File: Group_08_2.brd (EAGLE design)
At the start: 61 x 80 mm, 29 parts, among them J1 POWER_JACKPTH_LOCK, U1 +12v, U3 TCA9546ATSSOP, U4 TMUX1208

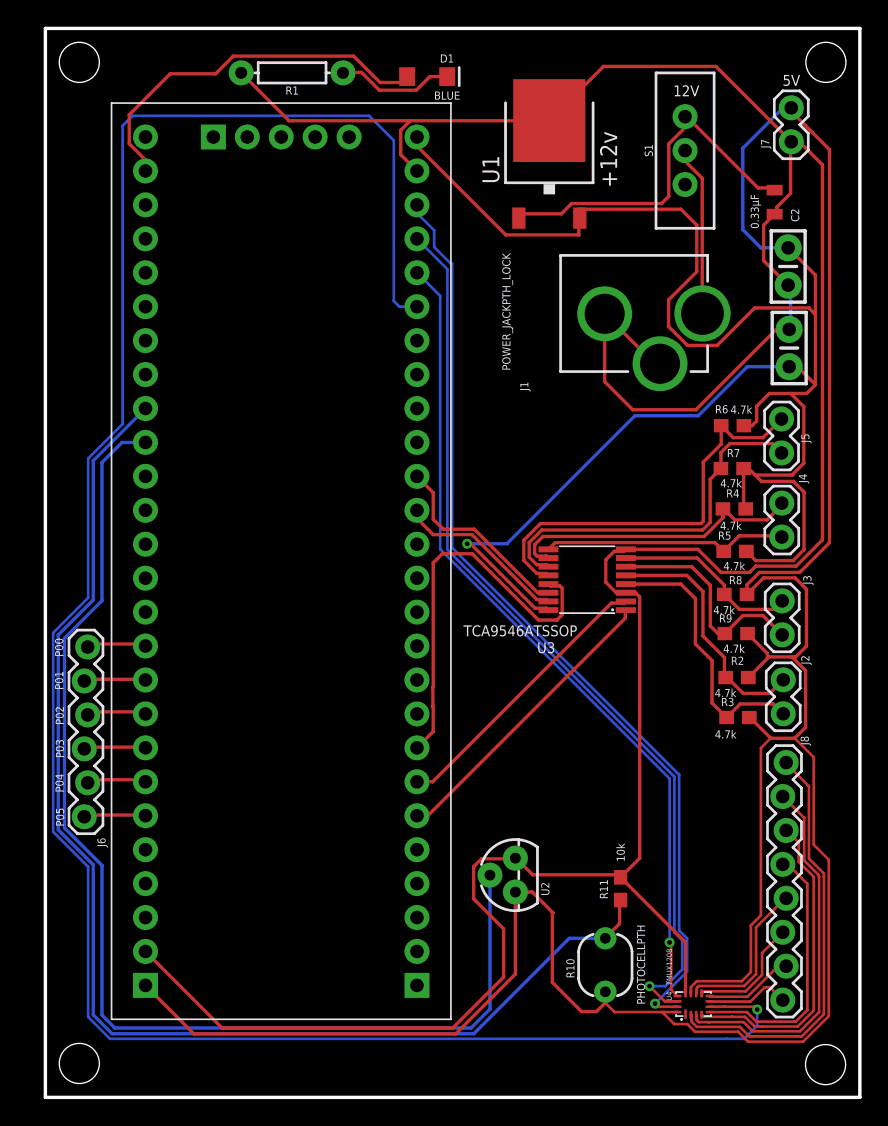
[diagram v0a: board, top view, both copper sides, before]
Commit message: completed routing of smaller board
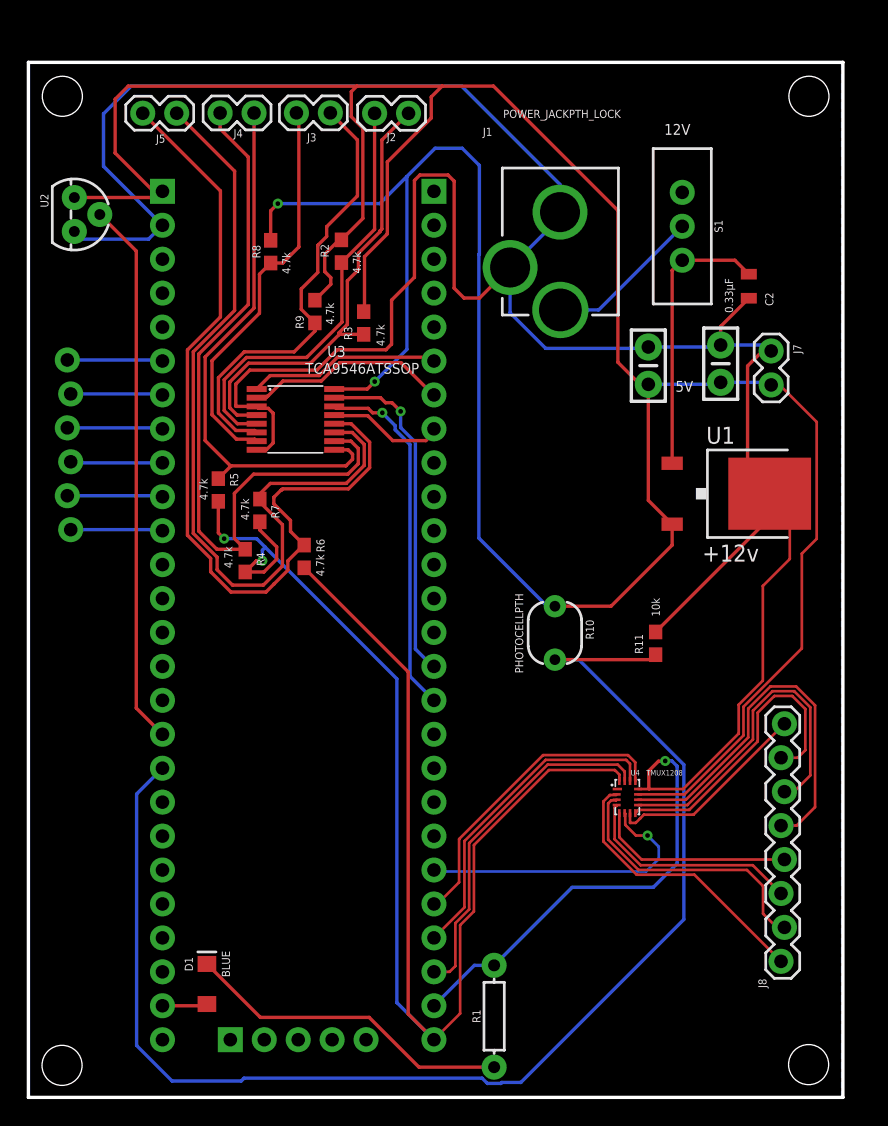
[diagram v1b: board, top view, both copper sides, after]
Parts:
- moved R1 72.2 mm to (34.9, 6.07), turned to 90 degrees
- moved D1 69.9 mm to (13.4, 8.49), turned to 90 degrees
- moved U2 59.5 mm to (3.44, 66.1), turned to 270 degrees
- moved J2 53.0 mm to (28.5, 73.7), turned to 180 degrees
- moved J5 51.9 mm to (11.1, 73.7), turned to 180 degrees
- moved J3 51.7 mm to (22.6, 73.7), turned to 180 degrees
- moved J4 50.7 mm to (16.9, 73.7), turned to 180 degrees
- moved R2 43.5 mm to (23.4, 63.3), turned to 90 degrees
- moved R8 43.2 mm to (18.1, 63.3), turned to 90 degrees
- moved R3 40.7 mm to (25.1, 58.0), turned to 90 degrees
- moved R9 39.7 mm to (21.4, 58.8), turned to 90 degrees
- moved R5 38.9 mm to (14.2, 45.5), turned to 270 degrees
- moved R4 36.8 mm to (16.2, 40.2), turned to 270 degrees
- moved R7 35.5 mm to (17.3, 43.9), turned to 270 degrees
- moved J6 34.2 mm to (2.91, 55.2), flipped to the bottom, turned to 270 degrees
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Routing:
- net MUX_OUT: track 161.3 -> 22.3 mm
- net 5V: track 336.6 -> 385.2 mm, vias 1 -> 4
- net TEMP_OUT: track 87.6 -> 40.8 mm
- net MUX_A0: track 71.0 -> 26.4 mm, vias 1 -> 0
- net MUX_A1: track 68.4 -> 24.5 mm, vias 1 -> 0
- net MUX_A2: track 62.2 -> 23.2 mm, vias 1 -> 0
- net I2C_SDA_3: track 27.7 -> 62.9 mm
- net I2C_SCL_3: track 31.0 -> 65.7 mm
- net I2C_SCL_2: track 22.8 -> 55.6 mm
- net N$26: track 28.3 -> 3.38 mm
- net I2C_SDA_2: track 18.5 -> 41.3 mm
- net I2C_A2: track 29.7 -> 8.79 mm
- net N$13: track 11.9 -> 29.3 mm
- net I2C_SDA_1: track 16.7 -> 34.1 mm
- net N$12: track 8.94 -> 25.7 mm
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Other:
- board size 61 x 80 mm -> 61 x 77.5 mm
- board text removed: "P00"
- board text removed: "P01"
- board text removed: "P02"
- board text removed: "P03"
- board text removed: "P04"
- board text removed: "P05"

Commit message: Adjustments to board file
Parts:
- moved U1 9.03 mm to (44.5, 42.0)
- moved C3 8.42 mm to (44.1, 51.5)
- moved C1 7.73 mm to (39.4, 51.4)
- moved J7 6.77 mm to (49.6, 52.7)
- moved J8 6.65 mm to (49.8, 27.4)
- moved C2 6.09 mm to (49.2, 56.8)
- moved R11 6.01 mm to (42.0, 30.6)
- moved U4 4.87 mm to (41.0, 19.5)
- moved R10 4.35 mm to (36.2, 31.9)
- moved J1 1.27 mm to (38.5, 72.8)
- moved J3 1.27 mm to (21.3, 73.7)
- moved R1 1.27 mm to (33.6, 6.07)
- moved D1 1.27 mm to (12.1, 8.49)
- moved J4 1.27 mm to (15.6, 73.7)
- moved R5 1.27 mm to (12.9, 45.5)
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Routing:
- net 5V: track 385.2 -> 430.2 mm
- net GND: track 233.1 -> 208.4 mm
- net PHOTO_OUT: track 101.1 -> 94.2 mm
- net 12V: track 20.9 -> 27.3 mm
- net MUX_OUT: track 22.3 -> 18.1 mm
- net N$17: track 20.6 -> 17.3 mm
- net N$14: track 14.9 -> 11.7 mm
- net N$16: track 16.8 -> 13.9 mm
- net N$10: track 15.4 -> 18.1 mm
- net MUX_A1: track 24.5 -> 21.8 mm
- net MUX_A2: track 23.2 -> 20.5 mm
- net MUX_A0: track 26.4 -> 23.9 mm
- net N$24: track 7.15 -> 4.81 mm
- net N$22: track 7.15 -> 4.81 mm
- net N$21: track 6.90 -> 4.56 mm
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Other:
- board size 61 x 77.5 mm -> 53.3 x 77.5 mm
